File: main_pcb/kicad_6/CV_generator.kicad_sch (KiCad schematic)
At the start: 35 parts, among them U10 SSI2162, U6 TL072, U7 TL072, U8 TL072

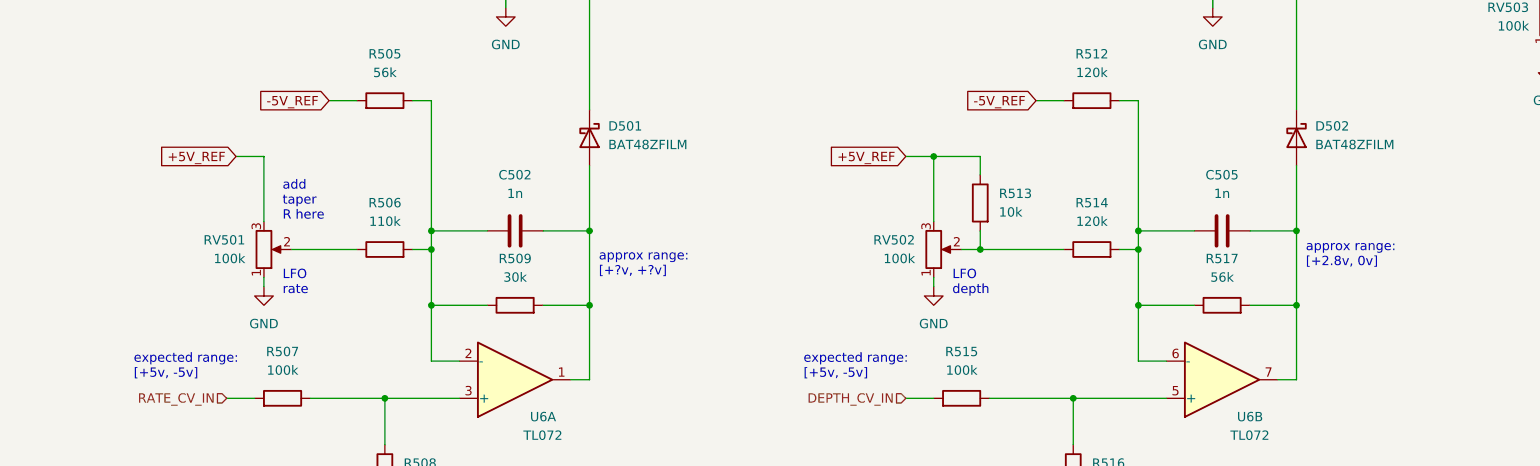
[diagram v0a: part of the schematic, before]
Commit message: Fix CV range notes in schem, add note about tapering R
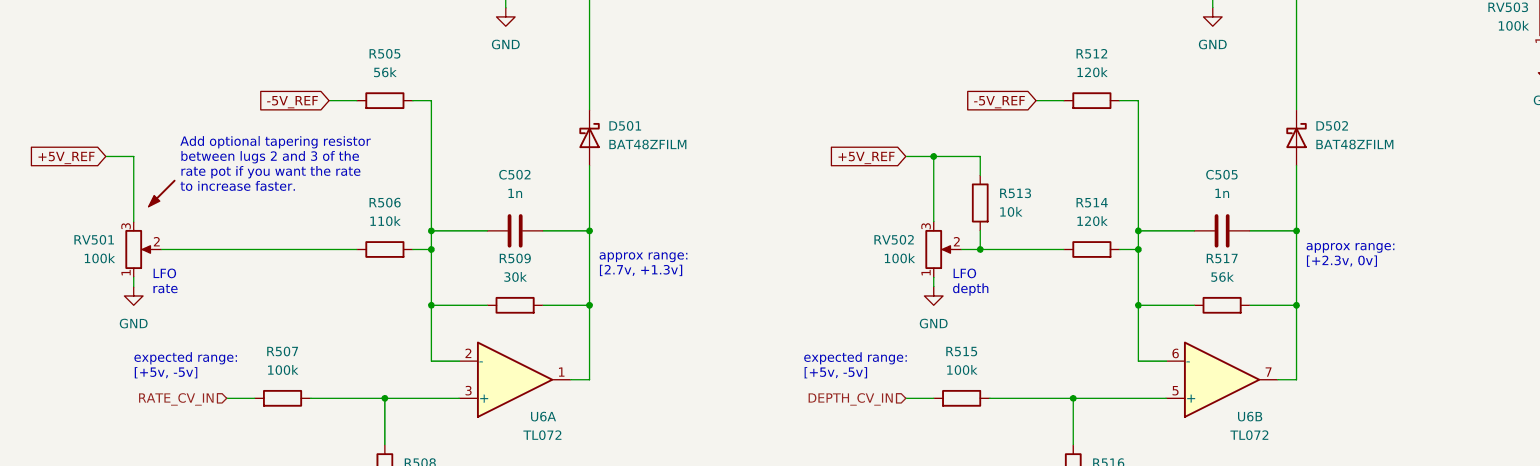
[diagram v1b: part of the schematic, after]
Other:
- note added: "Add optional tapering resistor between lugs 2 and 3 of the rate pot if you want the rate to increase faster."
- note added: "approx range: [+2.3v, 0v]"
- note added: "approx range: [2.7v, +1.3v]"
- note removed: "add taper R here"
- note removed: "approx range: [+2.8v, 0v]"
- note removed: "approx range: [+?v, +?v]"
- moved on the sheet: RV501
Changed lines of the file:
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@@
     (stroke (width 0) (type default) (color 0 0 0 0))
   )
-  (wire (pts (xy 49.53 129.54) (xy 58.42 129.54))
-    (stroke (width 0) (type default) (color 0 0 0 0))
-  )
-  (wire (pts (xy 45.72 134.62) (xy 45.72 133.35))
+  (wire (pts (xy 31.75 129.54) (xy 58.42 129.54))
+    (stroke (width 0) (type default) (color 0 0 0 0))
+  )
+  (wire (pts (xy 27.94 134.62) (xy 27.94 133.35))
     (stroke (width 0) (type default) (color 0 0 0 0))
   )
@@
     (stroke (width 0) (type default) (color 0 0 0 0))
   )
-  (wire (pts (xy 45.72 116.84) (xy 45.72 125.73))
+  (wire (pts (xy 27.94 116.84) (xy 27.94 125.73))
     (stroke (width 0) (type default) (color 0 0 0 0))
   )
@@
     (stroke (width 0) (type default) (color 0 0 0 0))
   )
-  (wire (pts (xy 41.91 116.84) (xy 45.72 116.84))
+  (wire (pts (xy 24.13 116.84) (xy 27.94 116.84))
     (stroke (width 0) (type default) (color 0 0 0 0))
   )
@@
     (stroke (width 0) (type default) (color 0 0 0 0))
   )
-  (text "approx range:\n[+?v, +?v]" (at 91.44 133.35 0)
+  (text "approx range:\n[2.7v, +1.3v]" (at 91.44 133.35 0)
     (effects (font (size 1.27 1.27)) (justify left bottom))
   )
@@
     (effects (font (size 3 3)) (justify left bottom))
   )
-  (text "approx range:\n[+2.8v, 0v]" (at 187.96 132.08 0)
-    (effects (font (size 1.27 1.27)) (justify left bottom))
-  )
-  (text "LFO\nrate" (at 48.26 135.89 0)
+  (text "approx range:\n[+2.3v, 0v]" (at 187.96 132.08 0)
+    (effects (font (size 1.27 1.27)) (justify left bottom))
+  )
+  (text "LFO\nrate" (at 30.48 135.89 0)
     (effects (font (size 1.27 1.27)) (justify left bottom))
   )
@@
     (effects (font (size 1.27 1.27)) (justify left bottom))
   )
-  (text "add\ntaper\nR here" (at 48.26 125.73 0)
+  (text "Add optional tapering resistor\nbetween lugs 2 and 3 of the \nrate pot if you want the rate \nto increase faster."
+    (at 34.29 121.92 0)
     (effects (font (size 1.27 1.27)) (justify left bottom))
   )
@@
     )
   )
-  (global_label "+5V_REF" (shape input) (at 41.91 116.84 180) (fields_autoplaced)
-    (effects (font (size 1.27 1.27)) (justify right))
-    (property "Intersheet References" "${INTERSHEET_REFS}" (id 0) (at 31.2401 116.7606 0)
+  (global_label "+5V_REF" (shape input) (at 24.13 116.84 180) (fields_autoplaced)
+    (effects (font (size 1.27 1.27)) (justify right))
+    (property "Intersheet References" "${INTERSHEET_REFS}" (id 0) (at 13.4601 116.7606 0)
       (effects (font (size 1.27 1.27)) (justify right) hide)
     )
@@
     (pin "1")
   )
-  (symbol (lib_id "Device:R_Potentiometer") (at 45.72 129.54 0) (mirror x) (unit 1)
-    (in_bom yes) (on_board yes) (fields_autoplaced)
-    (property "Reference" "RV501" (id 0) (at 43.18 128.2699 0)
+  (symbol (lib_id "Device:R_Potentiometer") (at 27.94 129.54 0) (mirror x) (unit 1)
+    (in_bom yes) (on_board yes) (fields_autoplaced)
+    (property "Reference" "RV501" (id 0) (at 25.4 128.2699 0)
       (effects (font (size 1.27 1.27)) (justify right))
     )
-    (property "Value" "100k" (id 1) (at 43.18 130.8099 0)
+    (property "Value" "100k" (id 1) (at 25.4 130.8099 0)
       (effects (font (size 1.27 1.27)) (justify right))
     )
-    (property "Footprint" "custom_footprints:Potentiometer_Alpha_RD901F-40-00D_Single_Vertical" (id 2) (at 45.72 129.54 0)
-      (effects (font (size 1.27 1.27)) hide)
-    )
-    (property "Datasheet" "~" (id 3) (at 45.72 129.54 0)
+    (property "Footprint" "custom_footprints:Potentiometer_Alpha_RD901F-40-00D_Single_Vertical" (id 2) (at 27.94 129.54 0)
+      (effects (font (size 1.27 1.27)) hide)
+    )
+    (property "Datasheet" "~" (id 3) (at 27.94 129.54 0)
       (effects (font (size 1.27 1.27)) hide)
     )
@@
     (pin "1")
   )
-  (symbol (lib_id "power:GND") (at 45.72 134.62 0) (mirror y) (unit 1)
-    (in_bom yes) (on_board yes) (fields_autoplaced)
-    (property "Reference" "#PWR0501" (id 0) (at 45.72 140.97 0)
-      (effects (font (size 1.27 1.27)) hide)
-    )
-    (property "Value" "GND" (id 1) (at 45.72 139.7 0))
-    (property "Footprint" "" (id 2) (at 45.72 134.62 0)
-      (effects (font (size 1.27 1.27)) hide)
-    )
-    (property "Datasheet" "" (id 3) (at 45.72 134.62 0)
+  (symbol (lib_id "power:GND") (at 27.94 134.62 0) (mirror y) (unit 1)
+    (in_bom yes) (on_board yes) (fields_autoplaced)
+    (property "Reference" "#PWR0501" (id 0) (at 27.94 140.97 0)
+      (effects (font (size 1.27 1.27)) hide)
+    )
+    (property "Value" "GND" (id 1) (at 27.94 139.7 0))
+    (property "Footprint" "" (id 2) (at 27.94 134.62 0)
+      (effects (font (size 1.27 1.27)) hide)
+    )
+    (property "Datasheet" "" (id 3) (at 27.94 134.62 0)
       (effects (font (size 1.27 1.27)) hide)
     )
@@
     (pin "8")
   )
+  (symbol (lib_id "Graphic:SYM_Arrow45_Normal") (at 31.75 121.92 270) (unit 1)
+    (in_bom yes) (on_board yes) (fields_autoplaced)
+    (property "Reference" "#SYM?" (id 0) (at 33.02 125.73 0)
+      (effects (font (size 1.27 1.27)) hide)
+    )
+    (property "Value" "SYM_Arrow45_Normal" (id 1) (at 29.21 121.92 0)
+      (effects (font (size 1.27 1.27)) hide)
+    )
+    (property "Footprint" "" (id 2) (at 31.75 121.92 0)
+      (effects (font (size 1.27 1.27)) hide)
+    )
+    (property "Datasheet" "~" (id 3) (at 31.75 121.92 0)
+      (effects (font (size 1.27 1.27)) hide)
+    )
+  )
   (symbol (lib_id "power:GND") (at 137.16 134.62 0) (mirror y) (unit 1)
